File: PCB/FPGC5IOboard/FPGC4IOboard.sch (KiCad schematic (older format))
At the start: 179 parts, among them J1 Conn_PS2_Mini_Din_6, J10 Conn_GPIO_Ext, J11 Conn_SPI_Ext, J12 Conn_Headphone_Jack, J13 Conn_W5500_1, J14 Conn_W5500_2, J4 Conn_NConfig, J6 Conn_Stacked_USB, J7 Conn_Debug_U8, J8 Conn_Debug_U7, J9 Conn_UART_Ext, Q1 BSS138, Q2 BSS138, Q3 BC847, Q4 BC847, SW1 SW_Push_Rst, SW2 SW_Slide, SW3 SW_Push_Config, U2 CH376T, U3 CH376T, U4 Conn_02x32_U7, U5 Conn_02x32_U8, U7 W25Q128JVS, U8 ESP32-WROOM-32U, U9 UDA1334ATS, Y1 12MHz, Y2 12MHz

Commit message: Initial version of PCBv3 schema is done
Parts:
- removed C26, C30, C31, C36, C?: 100nF, Capacitor_SMD:C_0805_2012Metric_Pad1.15x1.40mm_HandSolder, symbol FPGC4IOboard-rescue:C-Device
- removed C27, C29, C34: 10uF, Capacitor_SMD:C_0805_2012Metric_Pad1.15x1.40mm_HandSolder, symbol FPGC4IOboard-rescue:C-Device
- removed C32, C33: 47uF, Capacitor_THT:CP_Radial_D4.0mm_P2.00mm, symbol FPGC4IOboard-rescue:CP-Device
- removed C35: 1uF, Capacitor_SMD:C_0805_2012Metric_Pad1.15x1.40mm_HandSolder, symbol FPGC4IOboard-rescue:C-Device
- removed C37: 22uF, Capacitor_SMD:C_0805_2012Metric_Pad1.15x1.40mm_HandSolder, symbol FPGC4IOboard-rescue:C-Device
- removed C38, C39: 10nF, Capacitor_SMD:C_0805_2012Metric_Pad1.15x1.40mm_HandSolder, symbol FPGC4IOboard-rescue:C-Device
- removed C? (x2): 22pF, Capacitor_SMD:C_0805_2012Metric_Pad1.15x1.40mm_HandSolder, symbol FPGC4IOboard-rescue:C-Device
- removed D?: LED, symbol Device:LED
- removed D?: Red_LED, LED_SMD:LED_0805_2012Metric_Pad1.15x1.40mm_HandSolder, symbol FPGC4IOboard-rescue:LED-Device
- removed D?: Green_LED, LED_SMD:LED_0805_2012Metric_Pad1.15x1.40mm_HandSolder, symbol FPGC4IOboard-rescue:LED-Device
- removed J?: USB_B_Micro, RCJ013:MicroUSB_G30, symbol Connector:USB_B_Micro
- removed Q3, Q4: BC847, Package_TO_SOT_SMD:SOT-23, symbol FPGC4IOboard-rescue:BC847-Transistor_BJT
- removed R37, R38, R39, R40, R41, R42, R46, R58, R59, R? (x3): 10k, Resistor_SMD:R_0805_2012Metric_Pad1.15x1.40mm_HandSolder, symbol FPGC4IOboard-rescue:R-Device
- removed R43, R44, R45, R60, R61, R68, R69: 0, Resistor_SMD:R_0805_2012Metric_Pad1.15x1.40mm_HandSolder, symbol FPGC4IOboard-rescue:R-Device
- removed R47, R48: 220k, Resistor_SMD:R_0805_2012Metric_Pad1.15x1.40mm_HandSolder, symbol FPGC4IOboard-rescue:R-Device
- removed R49, R50: 100, Resistor_SMD:R_0805_2012Metric_Pad1.15x1.40mm_HandSolder, symbol FPGC4IOboard-rescue:R-Device
- removed R? (x2): 1k, Resistor_SMD:R_0805_2012Metric_Pad1.15x1.40mm_HandSolder, symbol FPGC4IOboard-rescue:R-Device
- removed U8: ESP32-WROOM-32U, RF_Module:ESP32-WROOM-32U, symbol FPGC4IOboard-rescue:ESP32-WROOM-32U-RF_Module
- removed U9: UDA1334ATS, Package_SO:SSOP-16_4.4x5.2mm_P0.65mm, symbol FPGC4IOboard-rescue:UDA1334ATS-Audio
- removed U?: CH340G, Package_SO:SOIC-16_3.9x9.9mm_P1.27mm, symbol Interface_USB:CH340G
- removed Y?: 12MHz, Crystal:Crystal_HC49-4H_Vertical, symbol FPGC4IOboard-rescue:Crystal-Device
- added C? (x3): 3.3uF, Capacitor_SMD:C_0805_2012Metric_Pad1.15x1.40mm_HandSolder, symbol FPGC4IOboard-rescue:C-Device
- added C?: 10uF, Capacitor_SMD:C_0805_2012Metric_Pad1.15x1.40mm_HandSolder, symbol FPGC4IOboard-rescue:C-Device
- added C? (x2): 2.7nF, Capacitor_SMD:C_0805_2012Metric_Pad1.15x1.40mm_HandSolder, symbol FPGC4IOboard-rescue:C-Device
- added C? (x2): 100nF, Capacitor_SMD:C_0805_2012Metric_Pad1.15x1.40mm_HandSolder, symbol FPGC4IOboard-rescue:C-Device
- added C?: 1uF, Capacitor_SMD:C_0805_2012Metric_Pad1.15x1.40mm_HandSolder, symbol FPGC4IOboard-rescue:C-Device
- added IC?: CS4344-CZZ, RCJ013:SOP50P490X110-10N, symbol CS4344-CZZ:CS4344-CZZ
- added R? (x2): 470, Resistor_SMD:R_0805_2012Metric_Pad1.15x1.40mm_HandSolder, symbol FPGC4IOboard-rescue:R-Device
- added R? (x2): 10k, Resistor_SMD:R_0805_2012Metric_Pad1.15x1.40mm_HandSolder, symbol FPGC4IOboard-rescue:R-Device
- added R? (x2): 0, Resistor_SMD:R_0805_2012Metric_Pad1.15x1.40mm_HandSolder, symbol FPGC4IOboard-rescue:R-Device
- F?: footprint Fuse:Fuse_1812_4532Metric_Pad1.30x3.40mm_HandSolder -> RCJ013:Fuse_1812
- J1: footprint Custom:Connector_Mini-DIN_Female_6Pin_2rows -> RCJ013:PS2
- SW?: footprint (none) -> RCJ013:SS12D06
- U2, U3: footprint SmallSMD:SSOP-20_5.3x7.2mm_P0.65mm -> RCJ013:SSOP-20_5.3x7.2mm_P0.65mm
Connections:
- net ESP32_RX2 is gone; now on net LED_USB1: U4.19 (Pin_19)
- net FPGC4_DTR is gone; now on net FPGC_DTR: U4.57 (Pin_57)
- net LED_NES is gone; now on net LED_VideoOutput: D?.1 (K)
- net LED_UARTapuRX is gone; now on net LED_FSX: D?.1 (K)
- net LED_UARTapuTX is gone; now on net LED_I2S: D?.1 (K)
- net Tip is gone; now on net Audio_Mono: J12.2 (Pin_2)
- net +3V3: now also C?.1, C?.1, IC?.9 (VA)
- net DAC_D0: now also U5.33 (Pin_33)
- net DAC_D1: now also U5.31 (Pin_31)
- net DAC_D2: now also U5.29 (Pin_29)
- net DAC_D3: now also U5.27 (Pin_27)
- net DAC_D4: now also U5.25 (Pin_25)
- net DAC_D5: now also U5.23 (Pin_23)
- net DAC_D6: now also U5.21 (Pin_21)
- net DAC_D7: now also U5.19 (Pin_19)
- net GND: now also C?.1, C?.2, C?.2, C?.2, C?.2, C?.2, C?.2, IC?.8 (GND), R?.1, R?.2
- net HDMI_CLK+: now also U5.47 (Pin_47)
- net HDMI_CLK-: now also U5.45 (Pin_45)
- net HDMI_D0+: now also U5.51 (Pin_51)
- net HDMI_D0-: now also U5.49 (Pin_49)
- net HDMI_D1+: now also U5.55 (Pin_55)
- net HDMI_D1-: now also U5.53 (Pin_53)
- net HDMI_D2+: now also U5.59 (Pin_59)
- net HDMI_D2-: now also U5.57 (Pin_57)
- net LED_Booted: now also U4.11 (Pin_11)
- net LED_Eth: now also U4.13 (Pin_13)
- net LED_Flash: now also U4.15 (Pin_15)
- net LED_PS2: now also U5.26 (Pin_26)
- net LED_SPImode: now also U5.22 (Pin_22)
- net LED_USB0: now also U4.17 (Pin_17)
- net LED_VideoOutput: now also U5.24 (Pin_24)
- net Ring1: now also R?.1
- net at U4.35 (Pin_35): now also J8.19 (Pin_19)
- net at U4.37 (Pin_37): now also J8.17 (Pin_17)
- net at U4.39 (Pin_39): now also J8.15 (Pin_15)
- net at U4.41 (Pin_41): now also J8.13 (Pin_13)
- net at U4.43 (Pin_43): now also J8.11 (Pin_11)
- net at U4.45 (Pin_45): now also J8.9 (Pin_9)
- net at U4.47 (Pin_47): now also J8.7 (Pin_7)
- net at U4.49 (Pin_49): now also J8.5 (Pin_5)
- net at U4.51 (Pin_51): now also J8.3 (Pin_3)
- net at U4.53 (Pin_53): now also J8.1 (Pin_1)
- net LED_I2S: now reaches U5.18 (Pin_18)
- net LED_FSX: now reaches U5.20 (Pin_20)
- net I2S_MCLK: now reaches U5.28 (Pin_28)
- net I2S_MCLK: now also IC?.4 (MCLK)
- net I2S_LRCLK: now reaches U5.30 (Pin_30)
- net I2S_LRCLK: now also IC?.3 (LRCK)
- net I2S_SCLK: now reaches U5.32 (Pin_32)
- net I2S_SCLK: now also IC?.2 (~DEM~/SCLK)
- net I2S_SDIN: now reaches U5.34 (Pin_34)
- net I2S_SDIN: now also IC?.1 (SDIN)
- net at U5.36 (Pin_36): now also J7.1 (Pin_1)
- net at U5.38 (Pin_38): now also J7.3 (Pin_3)
- net at U5.40 (Pin_40): now also J7.5 (Pin_5)
- net at U5.42 (Pin_42): now also J7.7 (Pin_7)
- net at U5.44 (Pin_44): now also J7.9 (Pin_9)
- net at U5.46 (Pin_46): now also J7.11 (Pin_11)
- net at U5.48 (Pin_48): now also J7.13 (Pin_13)
- net at U5.50 (Pin_50): now also J7.15 (Pin_15)
- net at U5.52 (Pin_52): now also J7.17 (Pin_17)
- net at U5.54 (Pin_54): now also J7.19 (Pin_19)
- net FPGC_DTR: now reaches U?.13 (~DTR)
- net CRT_AUDIO renamed Audio_Mono
- net Audio_Mono: now also R?.1
- net ESP32_TX2: no longer names the net of U4.21 (Pin_21)
- net FPGC4_RX renamed FPGC_RX
- net FPGC4_TX renamed FPGC_TX
- net USB_FPGC4_D1+ renamed USB_FPGC_D1+
- net USB_FPGC4_D1- renamed USB_FPGC_D1-
- net USB_FPGC4_D2+ renamed USB_FPGC_D2+
- net USB_FPGC4_D2- renamed USB_FPGC_D2-
- net VUSB: no longer names the net of J?.1 (VBUS), SW?.1
- new net: C?.1, IC?.10 (AOUTR)
- new net: C?.1, C?.1, IC?.5 (VQ)
- new net: C?.1, IC?.6 (FILT+)
- new net: C?.1, IC?.7 (AOUTL)
- new net: C?.2, R?.1, R?.2 (x2)
- new net: C?.2, R?.2, R?.2
- new net: C?.1, R?.1, R?.2
- no-connect marks 74 -> 44
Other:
- note added: "I2S-Audio"
- note removed: "Can move to the back now, since good USB keyboard support"
- note removed: "ESP32-I2S-Audio"
- note removed: "TODO: better physical switch"
- note removed: "TODO: look into adding 5v somewhere (like other development boards do)"
- note removed: "TODO: look into an alternative for audio"
- moved on the sheet: C?, D?, J12, J4, J7, J8, J?, R15, R17, R18, R6, R7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

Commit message: Ran annotation and fixed led footprints on schema
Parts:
- D1, D10, D2, D3, D4, D5, D6, D7, D8, D9: renamed from D?; footprint (none) -> LED_SMD:LED_0805_2012Metric_Pad1.15x1.40mm_HandSolder
- gave numbers to parts that had none: 71

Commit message: Fixed a bunch of footprints
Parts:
- C1, C11, C12, C13, C14, C15, C17, C18, C19, C2, C20, C21, C22, C23, C25, C26, C27, C28, C29, C3, C30, C31, C4, C5, C6, C8, C9: footprint Capacitor_SMD:C_0805_2012Metric_Pad1.15x1.40mm_HandSolder -> Capacitor_SMD:C_0805_2012Metric_Pad1.18x1.45mm_HandSolder
- J12: footprint Custom:TRRS-PJ-320A -> RCJ013:TRRS-PJ-320A
- J15: footprint Connector_USB:USB_Micro-B_Wuerth_629105150521 -> RCJ013:MicroUSB_G30
- R1, R10, R11, R12, R13, R14, R15, R16, R17, R18, R19, R2, R20, R21, R22, R23, R24, R25, R26, R27, R28, R29, R3, R30, R31, R32, R33, R34, R35, R36, R37, R38, R39, R4, R40, R41, R42, R43, R44, R45, R46, R47, R48, R49, R5, R50, R51, R52, R53, R54, R55, R56, R57, R58, R59, R6, R60, R61, R7, R70, R71, R72, R73, R8, R9: footprint Resistor_SMD:R_0805_2012Metric_Pad1.15x1.40mm_HandSolder -> Resistor_SMD:R_0805_2012Metric_Pad1.20x1.40mm_HandSolder
- U7: footprint Package_SO:SOIC-8_5.23x5.23mm_P1.27mm -> RCJ013:SOIC-8_5.23x5.23mm_P1.27mm

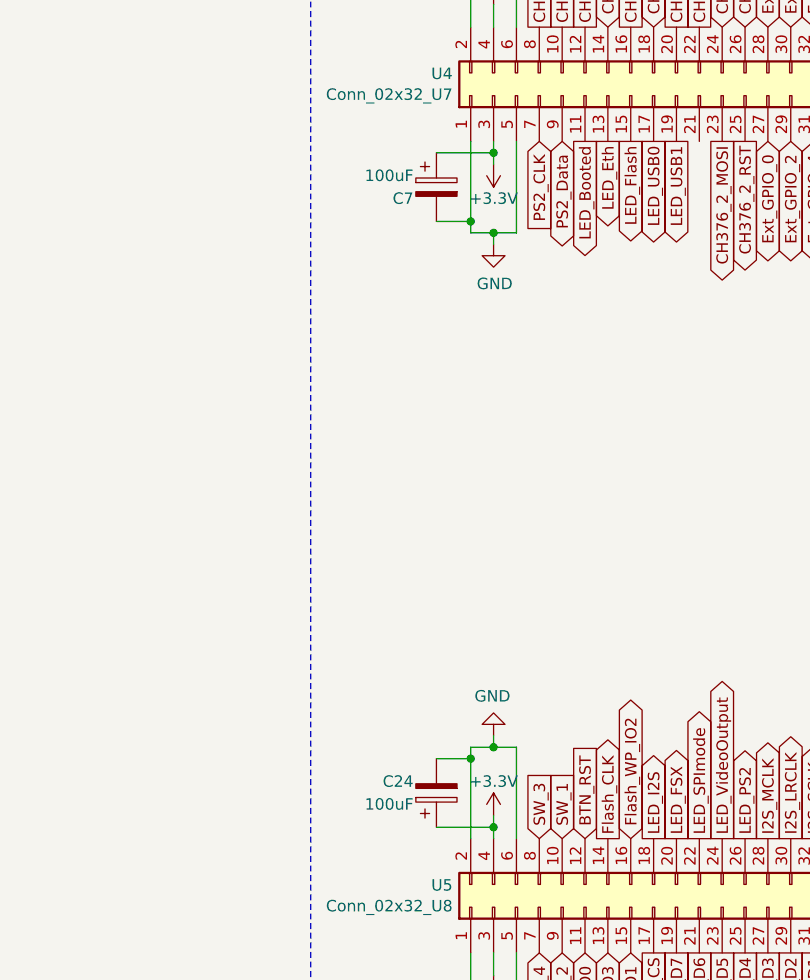
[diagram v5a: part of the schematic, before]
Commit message: Started on PCB layouting
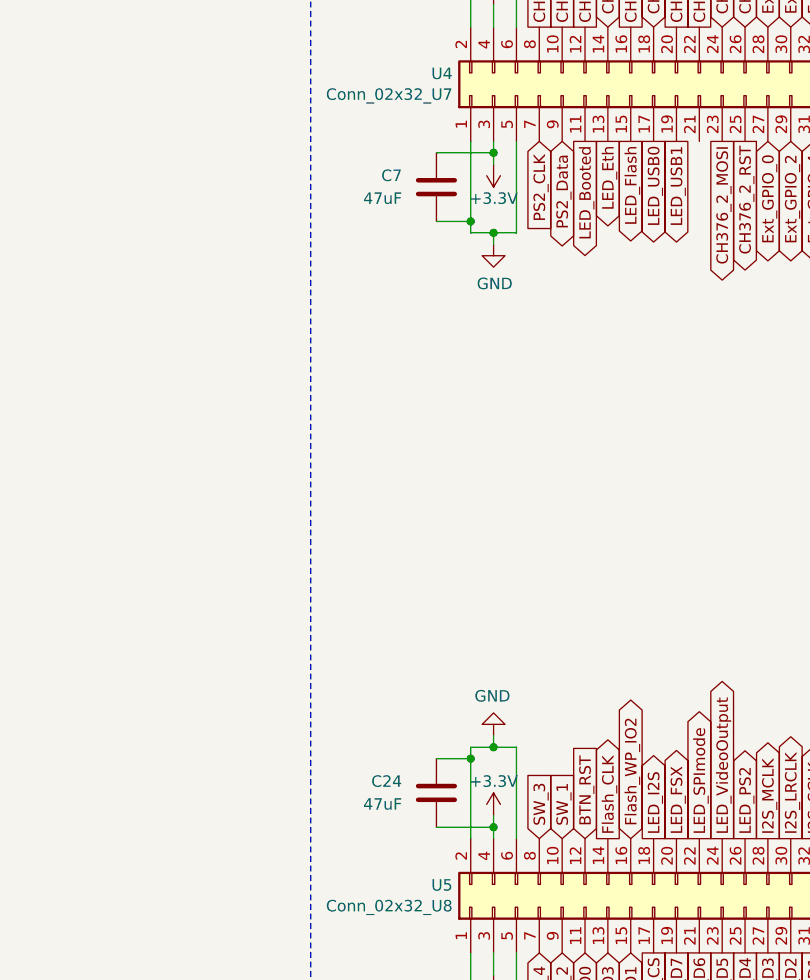
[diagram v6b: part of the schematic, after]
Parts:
- removed C24, C7: 100uF, Capacitor_THT:CP_Radial_D4.0mm_P2.00mm, symbol FPGC4IOboard-rescue:CP-Device
- added C24, C7: 47uF, Capacitor_SMD:C_0805_2012Metric_Pad1.18x1.45mm_HandSolder, symbol FPGC4IOboard-rescue:C-Device
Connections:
- net +3V3: now also C24.2, C7.1
- net GND: now also C24.1, C7.2
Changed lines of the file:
@@
 NoConn ~ 21250 10750
 $Comp
-L FPGC4IOboard-rescue:CP-Device C7
-U 1 1 5EE498A8
-P 9100 6850
-F 0 "C7" H 9000 6800 50  0000 R CNN
-F 1 "100uF" H 9000 6900 50  0000 R CNN
-F 2 "Capacitor_THT:CP_Radial_D4.0mm_P2.00mm" H 9138 6700 50  0001 C CNN
-F 3 "~" H 9100 6850 50  0001 C CNN
-	1    9100 6850
-	1    0    0    -1
-$EndComp
-$Comp
 L FPGC4IOboard-rescue:R-Device R35
 U 1 1 5E400D75
@@
 Wire Notes Line
 	14350 650  18500 650
-$Comp
-L FPGC4IOboard-rescue:CP-Device C24
-U 1 1 7E762AB8
-P 9100 9500
-F 0 "C24" H 9000 9450 50  0000 R CNN
-F 1 "100uF" H 9000 9550 50  0000 R CNN
-F 2 "Capacitor_THT:CP_Radial_D4.0mm_P2.00mm" H 9138 9350 50  0001 C CNN
-F 3 "~" H 9100 9500 50  0001 C CNN
-	1    9100 9500
-	1    0    0    1
-$EndComp
 Text GLabel 9650 6150 1    50   Output ~ 0
 CH376_1_CLK
@@
 	20200 10750 20100 10750
 Connection ~ 20100 10750
+$Comp
+L FPGC4IOboard-rescue:C-Device C24
+U 1 1 618519E9
+P 9100 9500
+F 0 "C24" H 9250 9550 50  0000 L CNN
+F 1 "47uF" H 9250 9450 50  0000 L CNN
+F 2 "Capacitor_SMD:C_0805_2012Metric_Pad1.18x1.45mm_HandSolder" H 9138 9350 50  0001 C CNN
+F 3 "~" H 9100 9500 50  0001 C CNN
+	1    9100 9500
+	-1   0    0    -1
+$EndComp
+$Comp
+L FPGC4IOboard-rescue:C-Device C7
+U 1 1 61858C87
+P 9100 6850
+F 0 "C7" H 9250 6900 50  0000 L CNN
+F 1 "47uF" H 9250 6800 50  0000 L CNN
+F 2 "Capacitor_SMD:C_0805_2012Metric_Pad1.18x1.45mm_HandSolder" H 9138 6700 50  0001 C CNN
+F 3 "~" H 9100 6850 50  0001 C CNN
+	1    9100 6850
+	-1   0    0    -1
+$EndComp
 $EndSCHEMATC

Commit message: PCB v3 initial routing done. Need to optimize and finish silkscreen layer
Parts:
- removed C10: 100uF, Capacitor_THT:CP_Radial_D4.0mm_P2.00mm, symbol FPGC4IOboard-rescue:CP-Device
- removed C11: 100nF, Capacitor_SMD:C_0805_2012Metric_Pad1.18x1.45mm_HandSolder, symbol FPGC4IOboard-rescue:C-Device
- removed J7: Conn_Debug_U8, Connector_PinHeader_2.54mm:PinHeader_2x10_P2.54mm_Vertical, symbol FPGC4IOboard-rescue:Conn_02x10_Odd_Even-Connector_Generic
- removed J8: Conn_Debug_U7, Connector_PinHeader_2.54mm:PinHeader_2x10_P2.54mm_Vertical, symbol FPGC4IOboard-rescue:Conn_02x10_Odd_Even-Connector_Generic
- removed R24, R27: 0, Resistor_SMD:R_0805_2012Metric_Pad1.20x1.40mm_HandSolder, symbol FPGC4IOboard-rescue:R-Device
- J3, J5: footprint RCJ013:CUI_RCJ-013 -> RCJ013:CUI_RCJ-013-Min
- R18: value 10K -> 0R
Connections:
- net +5V1 is gone; now on net +5V: C16.1, C17.2, J6.1 (Pin_1)
- net +5V2 is gone; now on net +5V: J6.5 (Pin_5)
- net +5V: now also C31.2, C32.1, SW4.2; no longer F1.2
- net BTN_RST: now also U4.15 (Pin_15); no longer U5.12 (Pin_12)
- net CH376_1_CLK: now also U4.8 (Pin_8); no longer U4.10 (Pin_10)
- net CH376_1_CS: now also U4.7 (Pin_7); no longer U4.8 (Pin_8)
- net CH376_1_INT: now also U4.10 (Pin_10); no longer U4.18 (Pin_18)
- net CH376_1_MISO: now also U4.12 (Pin_12); no longer U4.14 (Pin_14)
- net CH376_1_MOSI: now also U4.11 (Pin_11); no longer U4.12 (Pin_12)
- net CH376_1_RST: now also U4.9 (Pin_9); no longer U4.16 (Pin_16)
- net CH376_2_CS: now also U4.13 (Pin_13); no longer U4.20 (Pin_20)
- net CH376_2_INT: now also U4.19 (Pin_19); no longer U4.26 (Pin_26)
- net CH376_2_MISO: now also U4.21 (Pin_21); no longer U4.24 (Pin_24)
- net CH376_2_MOSI: now also U4.20 (Pin_20); no longer U4.23 (Pin_23)
- net CH376_2_RST: now also U4.17 (Pin_17); no longer U4.25 (Pin_25)
- net DAC_D0: now also U5.24 (Pin_24); no longer U5.33 (Pin_33)
- net DAC_D1: now also U5.26 (Pin_26); no longer U5.31 (Pin_31)
- net DAC_D2: now also U5.28 (Pin_28); no longer U5.29 (Pin_29)
- net DAC_D3: now also U5.30 (Pin_30); no longer U5.27 (Pin_27)
- net DAC_D4: now also U5.32 (Pin_32); no longer U5.25 (Pin_25)
- net DAC_D5: now also U5.34 (Pin_34); no longer U5.23 (Pin_23)
- net DAC_D6: now also U5.36 (Pin_36); no longer U5.21 (Pin_21)
- net DAC_D7: now also U5.38 (Pin_38); no longer U5.19 (Pin_19)
- net Ext_CLK: now also U5.11 (Pin_11); no longer U4.44 (Pin_44)
- net Ext_CS: now also U5.9 (Pin_9); no longer U4.46 (Pin_46)
- net Ext_GP: now also U5.7 (Pin_7); no longer U4.48 (Pin_48)
- net Ext_GPIO_0: now also U5.31 (Pin_31); no longer U4.27 (Pin_27)
- net Ext_GPIO_1: now also U5.29 (Pin_29); no longer U4.28 (Pin_28)
- net Ext_GPIO_2: now also U5.27 (Pin_27); no longer U4.29 (Pin_29)
- net Ext_GPIO_3: now also U5.25 (Pin_25); no longer U4.30 (Pin_30)
- net Ext_GPIO_4: now also U5.23 (Pin_23); no longer U4.31 (Pin_31)
- net Ext_GPIO_5: now also U5.21 (Pin_21); no longer U4.32 (Pin_32)
- net Ext_GPIO_6: now also U5.19 (Pin_19); no longer U4.33 (Pin_33)
- net Ext_GPIO_7: now also U5.17 (Pin_17); no longer U4.34 (Pin_34)
- net Ext_MISO: now also U5.15 (Pin_15); no longer U4.40 (Pin_40)
- net Ext_MOSI: now also U5.13 (Pin_13); no longer U4.42 (Pin_42)
- net Ext_RX: now also U4.34 (Pin_34); no longer U4.38 (Pin_38)
- net Ext_TX: now also U4.32 (Pin_32); no longer U4.36 (Pin_36)
- net FPGC_DTR: now also U4.53 (Pin_53); no longer U4.57 (Pin_57)
- net FPGC_RX: now also U4.51 (Pin_51); no longer U4.55 (Pin_55)
- net FPGC_TX: now also U4.49 (Pin_49); no longer U4.59 (Pin_59)
- net Flash_CLK: now also U4.43 (Pin_43); no longer U5.14 (Pin_14)
- net Flash_CS: now also U4.50 (Pin_50); no longer U5.17 (Pin_17)
- net Flash_HOLD_IO3: now also U4.39 (Pin_39); no longer U5.13 (Pin_13)
- net Flash_MISO_IO1: now also U4.45 (Pin_45); no longer U5.15 (Pin_15)
- net Flash_MOSI_IO0: now also U4.41 (Pin_41); no longer U5.11 (Pin_11)
- net Flash_WP_IO2: now also U4.47 (Pin_47); no longer U5.16 (Pin_16)
- net HDMI_CLK+: now also U1.4, U5.55 (Pin_55); no longer U1.1, U5.47 (Pin_47)
- net HDMI_CLK-: now also U1.3, U5.56 (Pin_56); no longer U1.6, U5.45 (Pin_45)
- net HDMI_D0+: now also U1.1, U5.53 (Pin_53); no longer U1.3, U5.51 (Pin_51)
- net HDMI_D0-: now also U1.6, U5.54 (Pin_54); no longer U1.4, U5.49 (Pin_49)
- net HDMI_D1+: now also U5.51 (Pin_51), U6.4; no longer U5.55 (Pin_55), U6.6
- net HDMI_D1-: now also U5.52 (Pin_52), U6.3; no longer U5.53 (Pin_53), U6.1
- net HDMI_D2+: now also U5.49 (Pin_49), U6.1; no longer U5.59 (Pin_59), U6.4
- net HDMI_D2-: now also U5.50 (Pin_50), U6.6; no longer U5.57 (Pin_57), U6.3
- net I2S_LRCLK: now also U4.31 (Pin_31); no longer U5.30 (Pin_30)
- net I2S_MCLK: now also U4.29 (Pin_29); no longer U5.28 (Pin_28)
- net I2S_SCLK: now also U4.33 (Pin_33); no longer U5.32 (Pin_32)
- net I2S_SDIN: now also U4.35 (Pin_35); no longer U5.34 (Pin_34)
- net LED_Booted: now also U4.23 (Pin_23); no longer U4.11 (Pin_11)
- net LED_Eth: now also U5.16 (Pin_16); no longer U4.13 (Pin_13)
- net LED_FSX: now also U5.12 (Pin_12); no longer U5.20 (Pin_20)
- net LED_Flash: now also U5.20 (Pin_20); no longer U4.15 (Pin_15)
- net LED_I2S: now also U5.10 (Pin_10); no longer U5.18 (Pin_18)
- net LED_PS2: now also U5.8 (Pin_8); no longer U5.26 (Pin_26)
- net LED_SPImode: now also U5.18 (Pin_18); no longer U5.22 (Pin_22)
- net LED_USB0: now also U4.25 (Pin_25); no longer U4.17 (Pin_17)
- net LED_USB1: now also U5.22 (Pin_22); no longer U4.19 (Pin_19)
- net LED_VideoOutput: now also U5.14 (Pin_14); no longer U5.24 (Pin_24)
- net PS2_CLK: now also U4.26 (Pin_26); no longer U4.7 (Pin_7)
- net PS2_Data: now also U4.28 (Pin_28); no longer U4.9 (Pin_9)
- net SW_1: now also U4.24 (Pin_24); no longer U5.10 (Pin_10)
- net SW_2: now also U4.18 (Pin_18); no longer U5.9 (Pin_9)
- net SW_3: now also U4.16 (Pin_16); no longer U5.8 (Pin_8)
- net SW_4: now also U4.14 (Pin_14); no longer U5.7 (Pin_7)
- net W5500_CLK: now also U4.59 (Pin_59); no longer U4.58 (Pin_58)
- net W5500_CS: now also U4.58 (Pin_58); no longer U4.56 (Pin_56)
- net W5500_INT: now also U4.57 (Pin_57); no longer U4.54 (Pin_54)
- net W5500_MISO: now also U4.55 (Pin_55); no longer U4.50 (Pin_50)
- net W5500_RST: now also U4.56 (Pin_56); no longer U4.52 (Pin_52)
- net at J15.1 (VBUS): now also F1.2; no longer SW4.1
- new net: F1.1, SW4.1
- no-connect marks 44 -> 57
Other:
- moved on the sheet: C31, C32, F1, SW4
